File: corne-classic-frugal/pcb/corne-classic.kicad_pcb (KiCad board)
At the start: 2 copper layers, 133.8 x 83.5 mm, 98 parts, among them J3 LED, P1 i2c-pin, P2 i2c-pin, SW1 SW_PUSH, SW10 SW_PUSH, SW11 SW_PUSH, SW12 SW_PUSH, SW13 SW_PUSH, SW14 SW_PUSH, SW15 SW_PUSH, SW16 SW_PUSH, SW17 SW_PUSH, SW18 SW_PUSH, SW19 SW_PUSH, SW2 SW_PUSH, SW20 SW_PUSH, SW21 SW_PUSH, SW3 SW_PUSH, SW4 SW_PUSH, SW5 SW_PUSH, SW6 SW_PUSH, SW7 SW_PUSH, SW8 SW_PUSH, SW9 SW_PUSH, U1 ProMicro

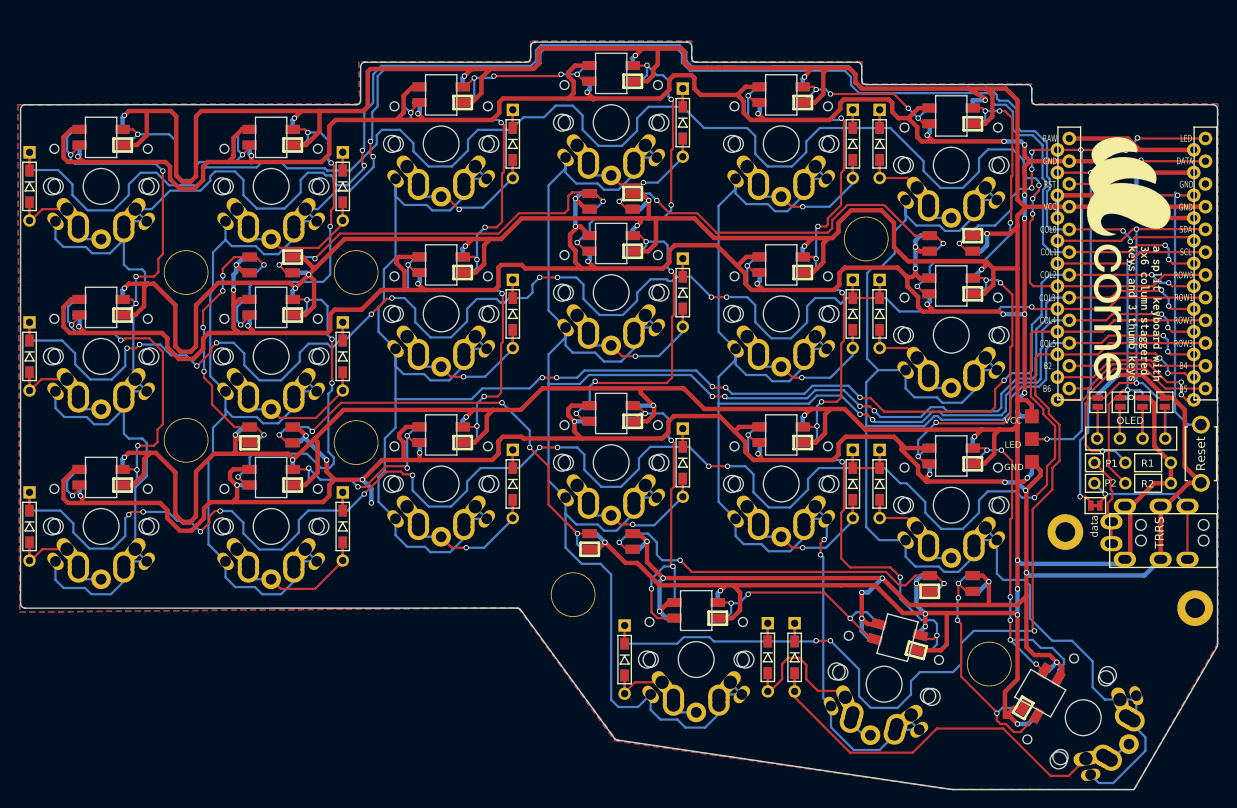
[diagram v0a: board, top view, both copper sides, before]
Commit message: temp: thumb layout and outline update. No routing yet.
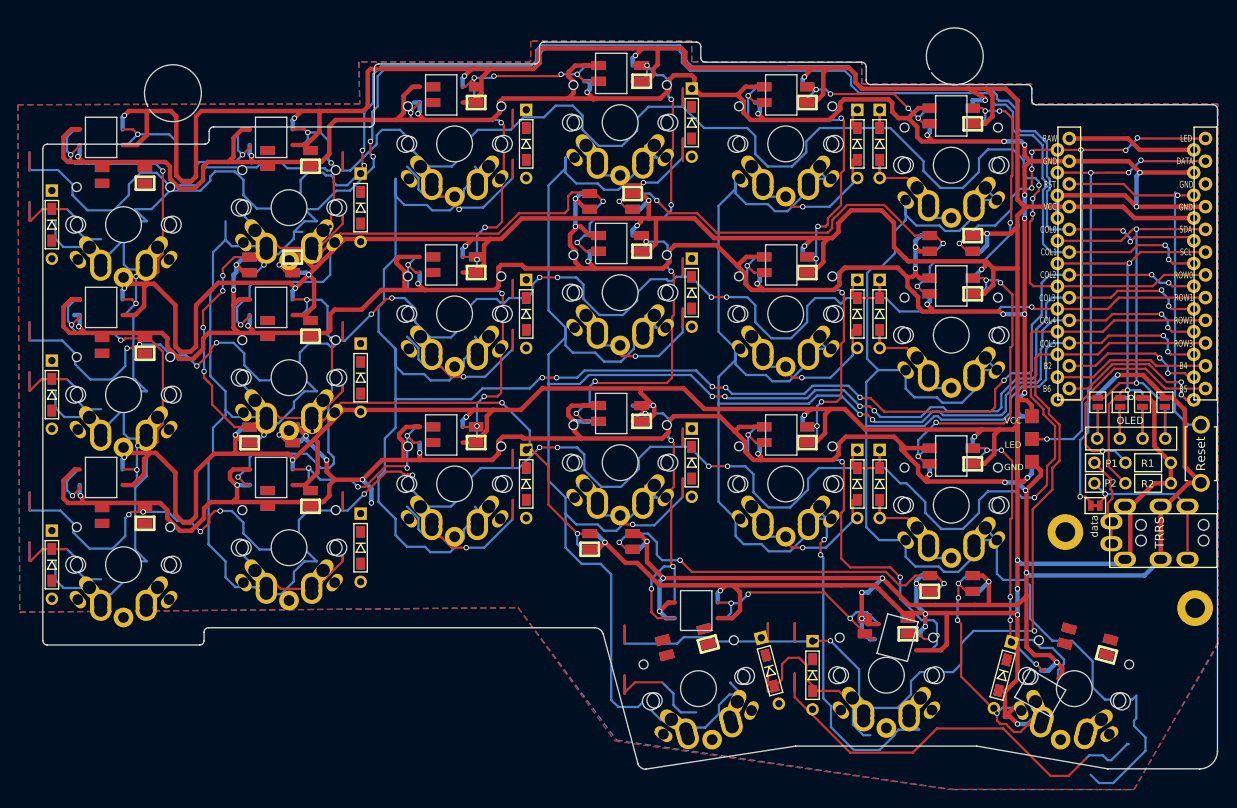
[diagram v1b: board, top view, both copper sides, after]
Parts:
- removed the ? at (79.5, 105.5)
- removed the ? at (79.5, 86.8)
- removed the ? at (98.5, 86.8)
- removed the ? at (98.5, 105.8)
- removed the ? at (155.5, 83.0)
- removed the ? at (122.8, 122.8)
- removed the ? at (169.2, 130.5)
- removed G*** (x2): LOGO, kbd:corne
- SW21: footprint kbd:MX_ALPS_PG1350_noLed_1.75u -> footprints:MX_ALPS_PG1350_noLed
- moved D21 23.3 mm to (170.8, 131.8), turned to 255 degrees
- moved D19 16.3 mm to (144.8, 131.2), turned to 285 degrees
- moved L21 7.79 mm to (180.2, 128.0), turned to 345 degrees
- moved D20 5.39 mm to (149.5, 131.8)
- moved D1 4.95 mm to (64.5, 81.4)
- moved D13 4.95 mm to (64.5, 119.4)
- moved D7 4.95 mm to (64.5, 100.4)
- moved L1 4.95 mm to (72.5, 75.9)
- moved L13 4.95 mm to (72.5, 113.9)
- moved L7 4.95 mm to (72.5, 94.9)
- moved SW1 4.95 mm to (72.5, 81.4)
- moved SW13 4.95 mm to (72.5, 119.4)
- moved SW7 4.95 mm to (72.5, 100.4)
- moved L19 3.75 mm to (135.3, 128.1), turned to 15 degrees
- moved SW21 3.40 mm to (178.8, 133.2), turned to 165 degrees
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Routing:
- net Net-(L17-Pad1): track 49.6 -> 0.00 mm, vias 4 -> 0
- net (no net): track 0.00 -> 49.6 mm, vias 0 -> 4
- net col5: track 187.4 -> 235.3 mm
- net Net-(D21-Pad2): track 49.9 -> 2.03 mm
- net col0: track 245.7 -> 282.8 mm, vias 4 -> 8
- net Net-(L13-Pad3): track 37.1 -> 0.00 mm, vias 4 -> 0
- net Net-(L19-Pad3): track 27.9 -> 0.00 mm, vias 3 -> 0
- net VCC: track 758.2 -> 786.0 mm, vias 33 -> 36
- net col2: track 197.5 -> 209.4 mm
- net Net-(D9-Pad2): track 20.2 -> 14.3 mm
- net Net-(D15-Pad2): track 20.2 -> 14.2 mm
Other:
- board size 133.8 x 83.5 mm -> 131.3 x 82.8 mm
- board text added: "Based on “Corne Classic” v2.0 by foostan"
- board text added: "v0.1 2018-10-06 by ryo1kato@"

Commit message: layout and edges. No routes yet.
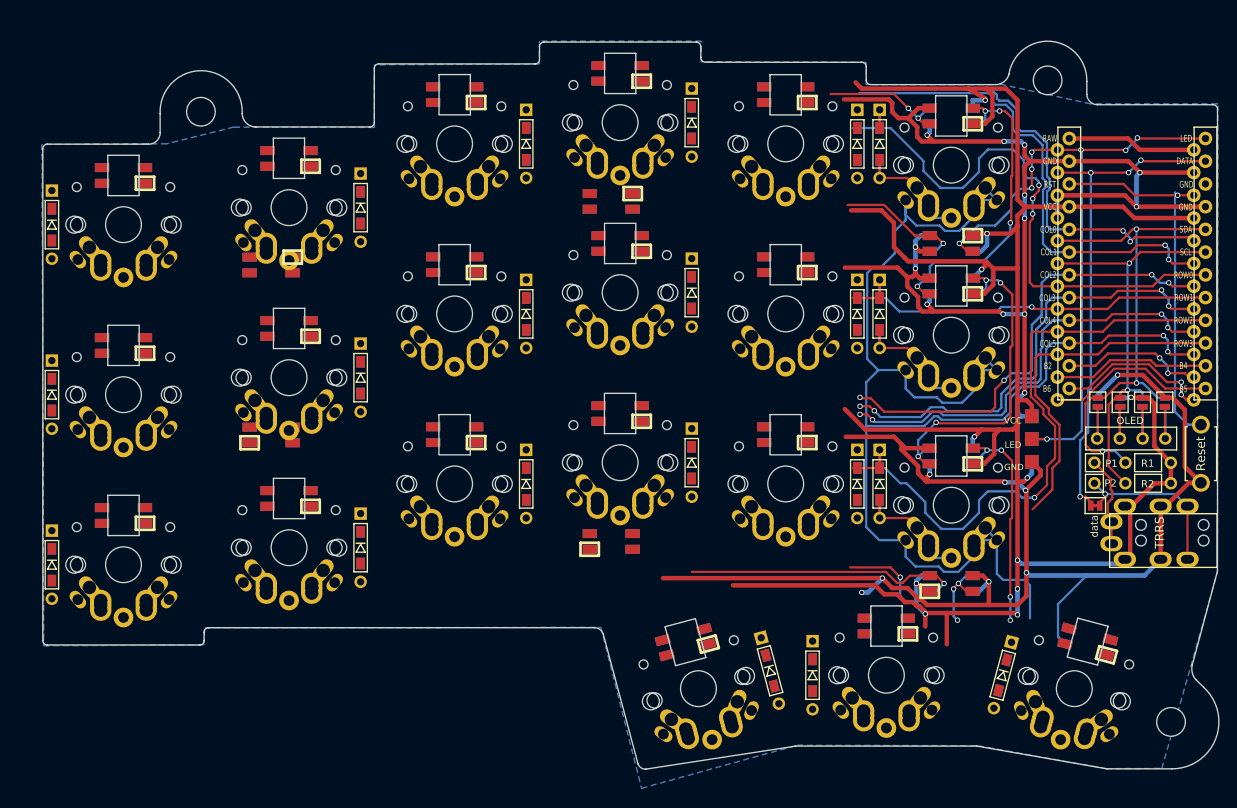
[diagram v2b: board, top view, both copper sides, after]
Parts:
- removed ? (x2): , kbd:LEGO_HOLE
- added REF01: MountingHole_3.2mm_M3, MountingHole:MountingHole_3.2mm_M3, F.Cu at (175.8, 65.3)
- added REF02: MountingHole_3.2mm_M3, MountingHole:MountingHole_3.2mm_M3, F.Cu at (81.2, 68.8)
- added REF03: , MountingHole:MountingHole_3.2mm_M3, F.Cu at (189.6, 137.0)
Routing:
- net VCC: track 786.0 -> 265.7 mm, vias 36 -> 11
- net GND: track 797.7 -> 305.4 mm, vias 49 -> 21
- net col0: track 282.8 -> 51.9 mm, vias 8 -> 2
- net col3: track 225.2 -> 50.4 mm, vias 6 -> 4
- net col1: track 222.0 -> 54.8 mm, vias 4 -> 2
- net col2: track 209.4 -> 51.0 mm, vias 8 -> 4
- net row1: track 191.7 -> 44.9 mm, vias 11 -> 1
- net col4: track 194.3 -> 48.3 mm, vias 6 -> 4
- net row2: track 215.8 -> 71.2 mm, vias 11 -> 1
- net row0: track 205.5 -> 65.4 mm
- net row3: track 121.8 -> 39.0 mm, vias 3 -> 0
- net col5: track 235.3 -> 155.1 mm
- net Net-(L25-Pad1): track 51.6 -> 0.00 mm, vias 5 -> 0
- net (no net): track 49.6 -> 0.00 mm, vias 4 -> 0
- net Net-(L22-Pad3): track 45.1 -> 0.00 mm, vias 3 -> 0
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- removed copper zone on F.Cu, net GND
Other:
- board size 131.3 x 82.8 mm -> 131.4 x 81.3 mm
- board text removed: "Corne Classic v2.0 PCB Designed by foostan"
- board text removed: "v0.1 2018-10-06 by ryo1kato@"

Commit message: work until now - key matrix tracks are done. LEDs are half way
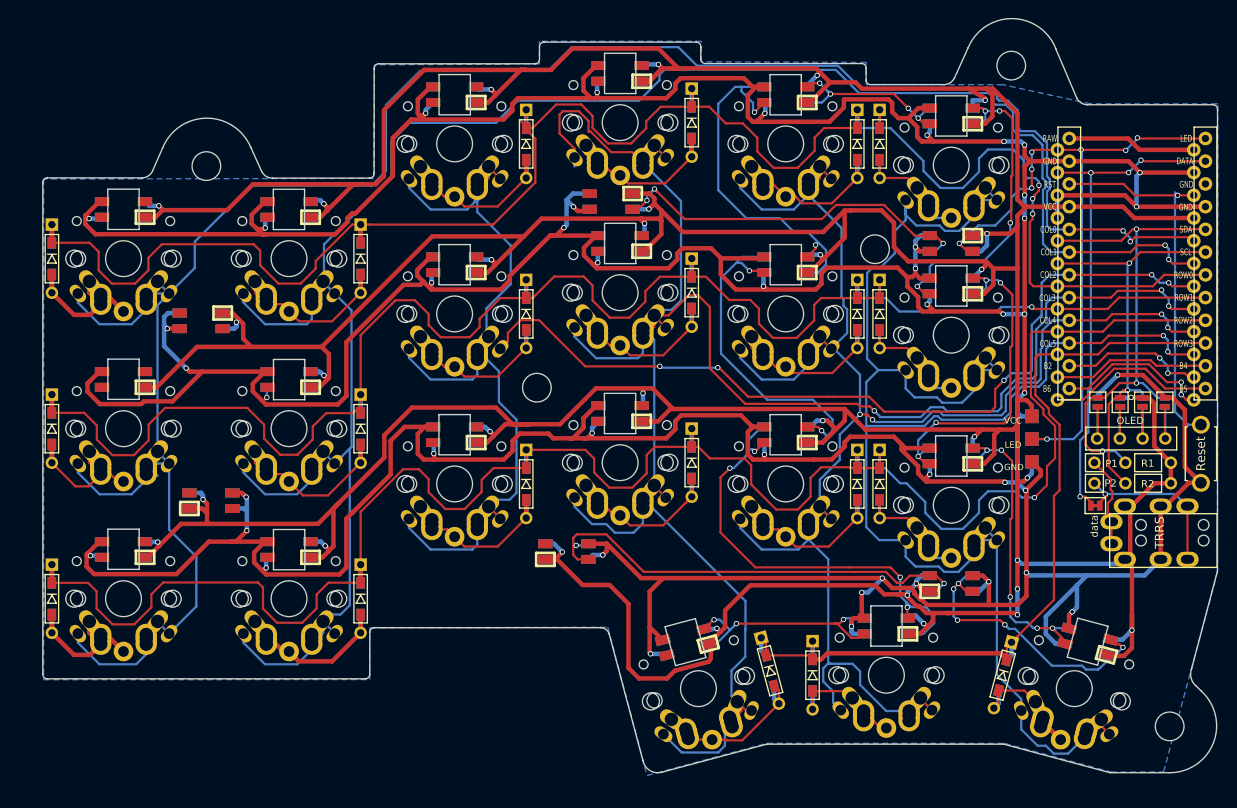
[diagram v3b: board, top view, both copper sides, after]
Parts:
- added REF01: MountingHole_3.2mm_M3, MountingHole:MountingHole_3.2mm_M3, F.Cu at (156.5, 84.1)
- added REF01: MountingHole_3.2mm_M3, MountingHole:MountingHole_3.2mm_M3, F.Cu at (118.7, 99.6)
- moved L22 10.0 mm to (81.2, 92.2)
- moved L25 9.96 mm to (82.3, 112.2)
- moved REF02 6.10 mm to (81.8, 74.9)
- moved D14 5.70 mm to (99.0, 123.2)
- moved D2 5.70 mm to (99.0, 85.2)
- moved D8 5.70 mm to (99.0, 104.2)
- moved L14 5.70 mm to (91.0, 117.7)
- moved L2 5.70 mm to (91.0, 79.7)
- moved L8 5.70 mm to (91.0, 98.7)
- moved SW14 5.70 mm to (91.0, 123.2)
- moved SW2 5.70 mm to (91.0, 85.2)
- moved SW8 5.70 mm to (91.0, 104.2)
- moved L26 5.08 mm to (122.0, 117.9)
- moved REF01 4.39 mm to (171.7, 63.6)
- moved D1 3.80 mm to (64.5, 85.2)
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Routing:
- net GND: track 305.4 -> 791.4 mm, vias 21 -> 45
- net VCC: track 265.7 -> 735.5 mm, vias 11 -> 32
- net col0: track 51.9 -> 239.9 mm
- net col3: track 50.4 -> 226.9 mm, vias 4 -> 3
- net col1: track 54.8 -> 224.8 mm
- net row1: track 44.9 -> 195.0 mm
- net row2: track 71.2 -> 219.8 mm
- net row0: track 65.4 -> 210.5 mm
- net col2: track 51.0 -> 183.6 mm, vias 4 -> 5
- net col4: track 48.3 -> 177.1 mm
- net row3: track 39.0 -> 95.3 mm
- net Net-(L17-Pad1): track 8.46 -> 51.6 mm, vias 1 -> 4
- net Net-(L11-Pad3): track 0.00 -> 41.6 mm, vias 0 -> 2
- net Net-(L11-Pad1): track 0.00 -> 40.8 mm, vias 0 -> 2
- net Net-(L23-Pad3): track 15.1 -> 44.3 mm, vias 1 -> 3
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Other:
- board size 131.4 x 81.3 mm -> 131.3 x 84.3 mm

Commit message: first version with all routing completed
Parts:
- moved REF01 2.18 mm to (155.2, 82.3)
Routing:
- net Net-(L22-Pad3): track 0.00 -> 63.3 mm, vias 0 -> 2
- net Net-(L3-Pad1): track 0.00 -> 47.3 mm, vias 0 -> 6
- net Net-(L25-Pad1): track 0.00 -> 46.5 mm, vias 0 -> 3
- net Net-(L16-Pad3): track 0.00 -> 45.4 mm, vias 0 -> 2
- net Net-(L15-Pad3): track 0.00 -> 38.8 mm, vias 0 -> 2
- net Net-(L14-Pad1): track 0.00 -> 38.5 mm, vias 0 -> 4
- net Net-(L10-Pad1): track 0.00 -> 38.5 mm, vias 0 -> 4
- net Net-(L1-Pad1): track 0.00 -> 38.4 mm, vias 0 -> 2
- net Net-(L13-Pad3): track 0.00 -> 36.9 mm, vias 0 -> 2
- net Net-(L10-Pad3): track 0.00 -> 36.9 mm, vias 0 -> 2
- net Net-(L2-Pad3): track 0.00 -> 35.0 mm, vias 0 -> 2
- net Net-(L14-Pad3): track 0.00 -> 32.4 mm, vias 0 -> 4
- net GND: track 791.4 -> 823.6 mm, vias 45 -> 66
- net Net-(L22-Pad1): track 0.00 -> 30.5 mm, vias 0 -> 2
- net Net-(L1-Pad3): track 0.00 -> 23.4 mm, vias 0 -> 4
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- added copper zone on F.Cu, net GND

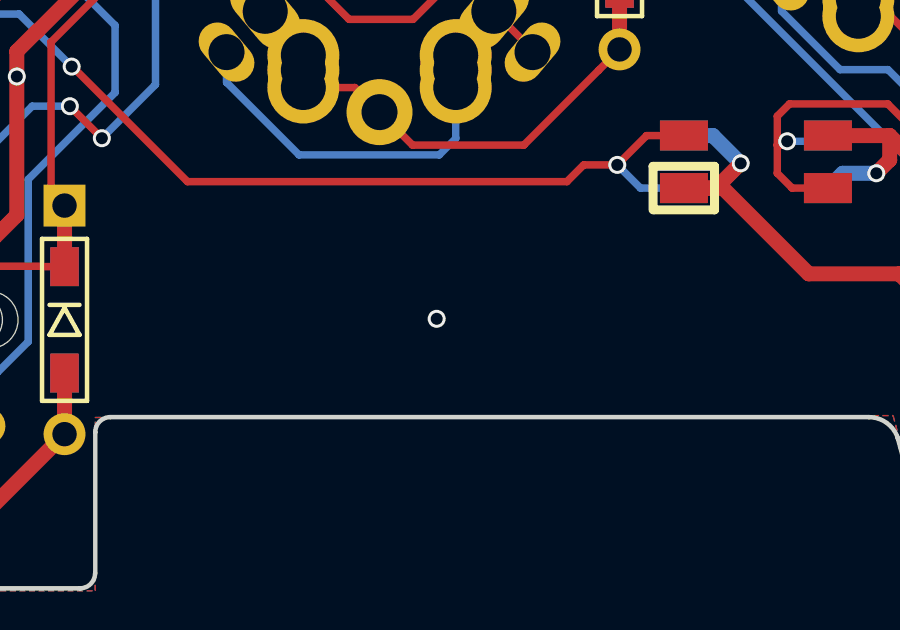
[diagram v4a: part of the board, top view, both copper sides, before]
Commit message: adding board name string
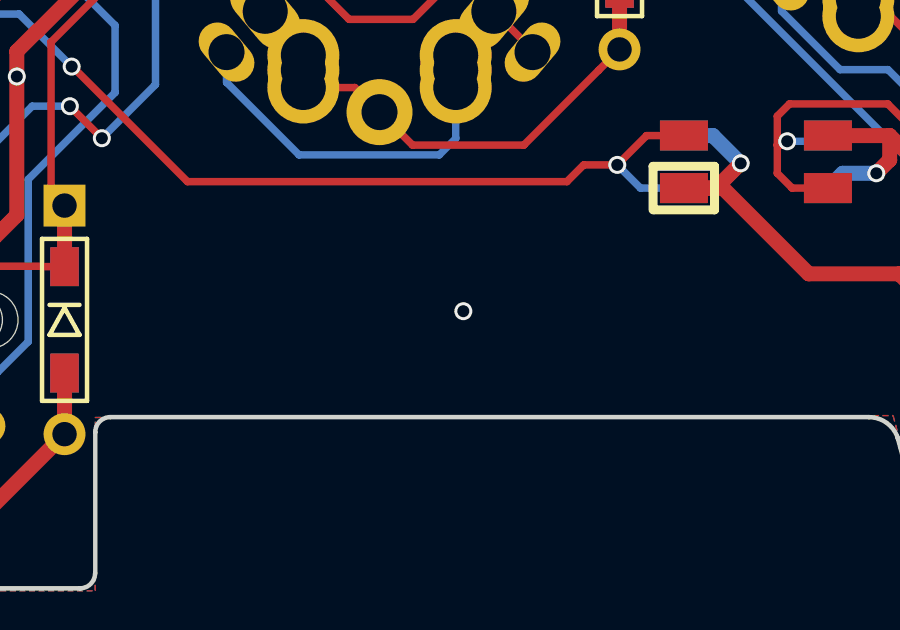
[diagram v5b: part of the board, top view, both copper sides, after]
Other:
- board text added: "TinyPinky42 v0.1 PCB design by ryo1kato@"
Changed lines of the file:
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@@
   (general
     (thickness 1.6)
-    (drawings 145)
+    (drawings 146)
     (tracks 2813)
     (zones 0)
@@
     (41 Cmts.User user)
     (42 Eco1.User user)
-    (43 Eco2.User user hide)
+    (43 Eco2.User user)
     (44 Edge.Cuts user)
     (45 Margin user)
@@
     (47 F.CrtYd user)
     (48 B.Fab user)
-    (49 F.Fab user hide)
+    (49 F.Fab user)
   )
   (setup
@@
     (pad 1 np_thru_hole circle (at 0 0) (size 3.2 3.2) (drill 3.2) (layers *.Cu *.Mask))
   )
+  (gr_text "TinyPinky42 v0.1\nPCB design by ryo1kato@" (at 113.1316 122.6312) (layer B.Mask)
+    (effects (font (size 1.5 1.3) (thickness 0.15)) (justify mirror))
+  )
+  (gr_text "TinyPinky42 v0.1\nPCB design by ryo1kato@" (at 113.3348 122.5804) (layer F.Mask)
+    (effects (font (size 1.5 1.3) (thickness 0.15)))
+  )
   (gr_arc (start 89.130658 74.876679) (end 89.156058 76.197479) (angle 65.95690606) (layer Edge.Cuts) (width 0.15))
   (gr_arc (start 74.546942 74.851279) (end 74.521542 76.172079) (angle -65.95690606) (layer Edge.Cuts) (width 0.15))
@@
     (effects (font (size 0.7 0.7) (thickness 0.125)))
   )
-  (target plus (at 194.8 63.4) (size 5) (width 0.15) (layer Edge.Cuts))
   (gr_text "Based on “Corne Classic” v2.0\nby foostan" (at 184.92724 95.92818 90) (layer F.Mask)
     (effects (font (size 1 1) (thickness 0.125)) (justify left))
@@
   (via (at 73.787 112.8014) (size 0.6) (drill 0.4) (layers F.Cu B.Cu) (net 26))
   (via (at 72.644 93.5736) (size 0.6) (drill 0.4) (layers F.Cu B.Cu) (net 26))
-  (via (at 111.4044 123.1646) (size 0.6) (drill 0.4) (layers F.Cu B.Cu) (net 26))
+  (via (at 112.2934 122.9106) (size 0.6) (drill 0.4) (layers F.Cu B.Cu) (net 26))
   (via (at 132.8166 117.3734) (size 0.6) (drill 0.4) (layers F.Cu B.Cu) (net 26))
   (via (at 81.6356 127.9398) (size 0.6) (drill 0.4) (layers F.Cu B.Cu) (net 26))

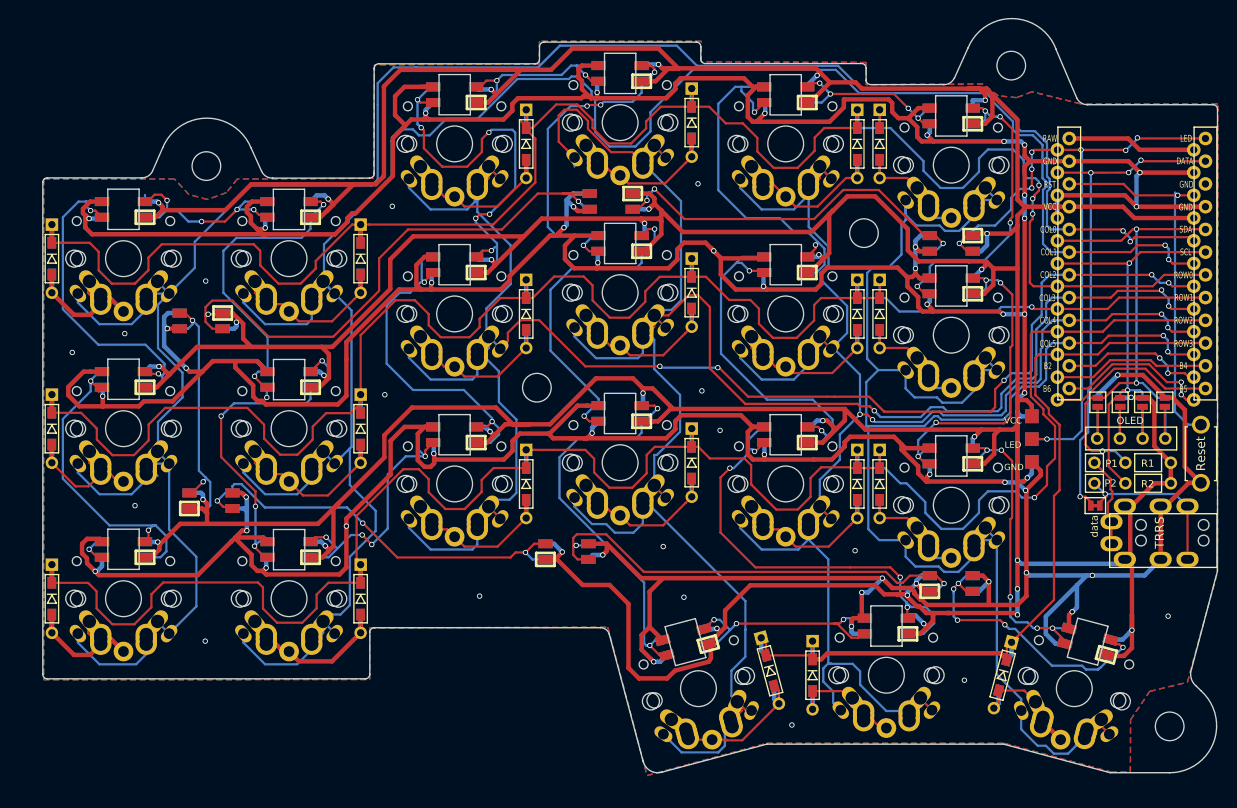
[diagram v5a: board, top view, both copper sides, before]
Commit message: additional connection between keyswitch thru-holes
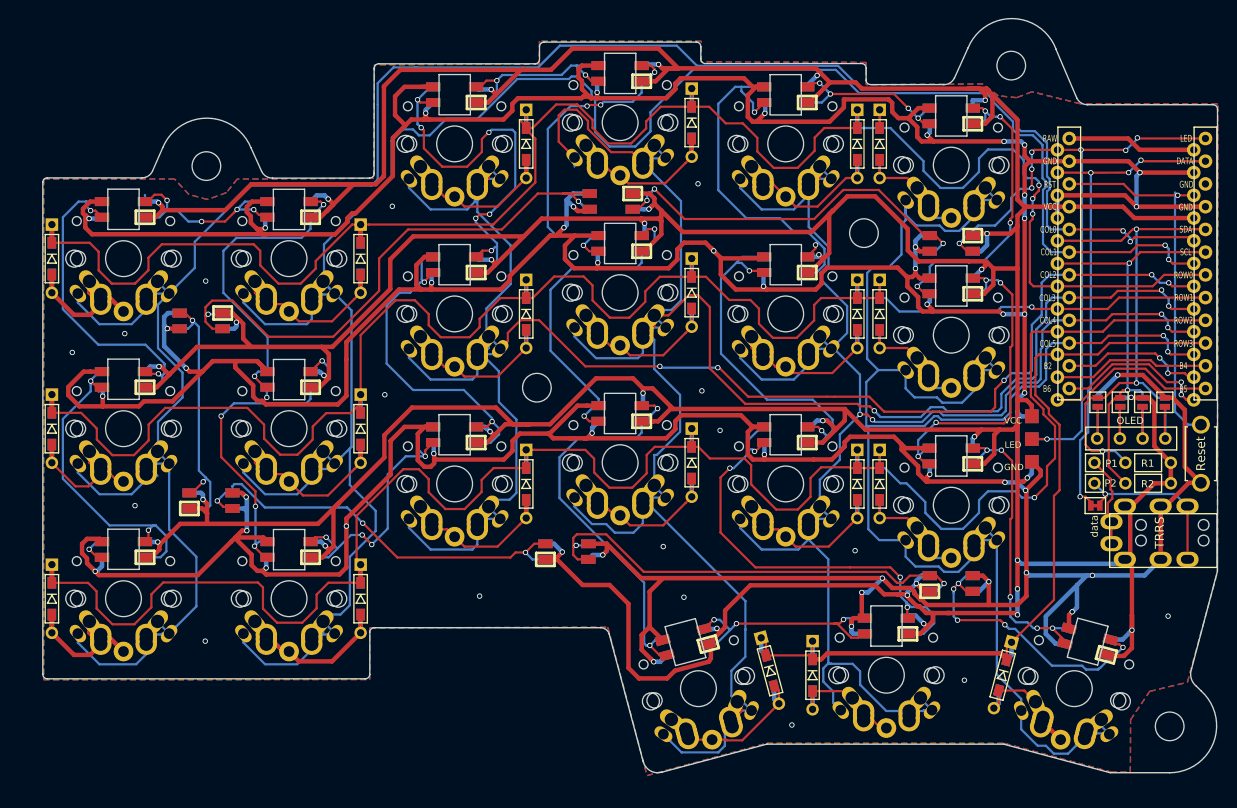
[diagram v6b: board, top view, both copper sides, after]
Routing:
- net col4: track 177.8 -> 188.6 mm
- net col3: track 229.5 -> 240.1 mm
- net col2: track 190.6 -> 198.8 mm
- net col1: track 236.2 -> 244.2 mm
- net col5: track 180.0 -> 182.7 mm
- net col0: track 243.8 -> 246.4 mm
